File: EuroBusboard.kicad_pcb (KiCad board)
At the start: 2 copper layers, 146 x 70 mm, 39 parts, among them J1 Power In, J10 IDC5, J11 JST5, J12 IDC6, J13 JST6, J14 IDC7, J15 JST7, J16 IDC8, J17 JST8, J18 Power thru, J19 Power In, J2 IDC1, J20 Power thru, J21 Power Thru, J22 Power In, J3 JST1, J4 IDC2, J5 JST2, J6 IDC3, J7 JST3, J8 IDC4, J9 JST4

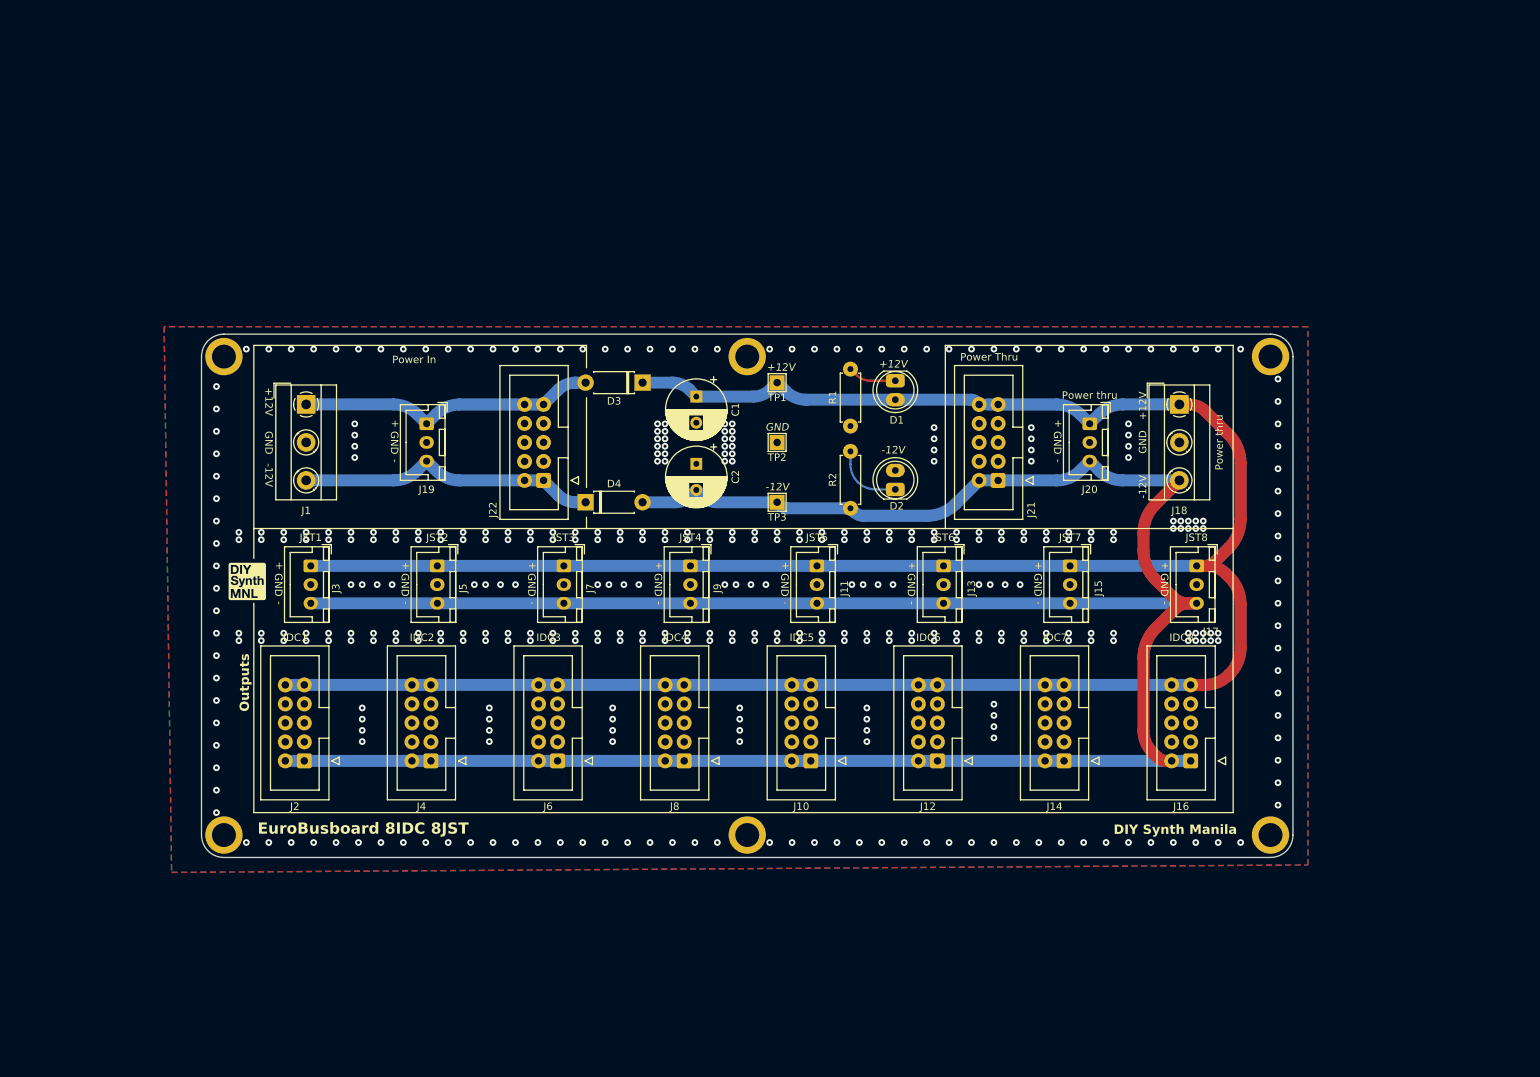
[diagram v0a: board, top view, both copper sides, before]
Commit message: added idc and jst only bus boards
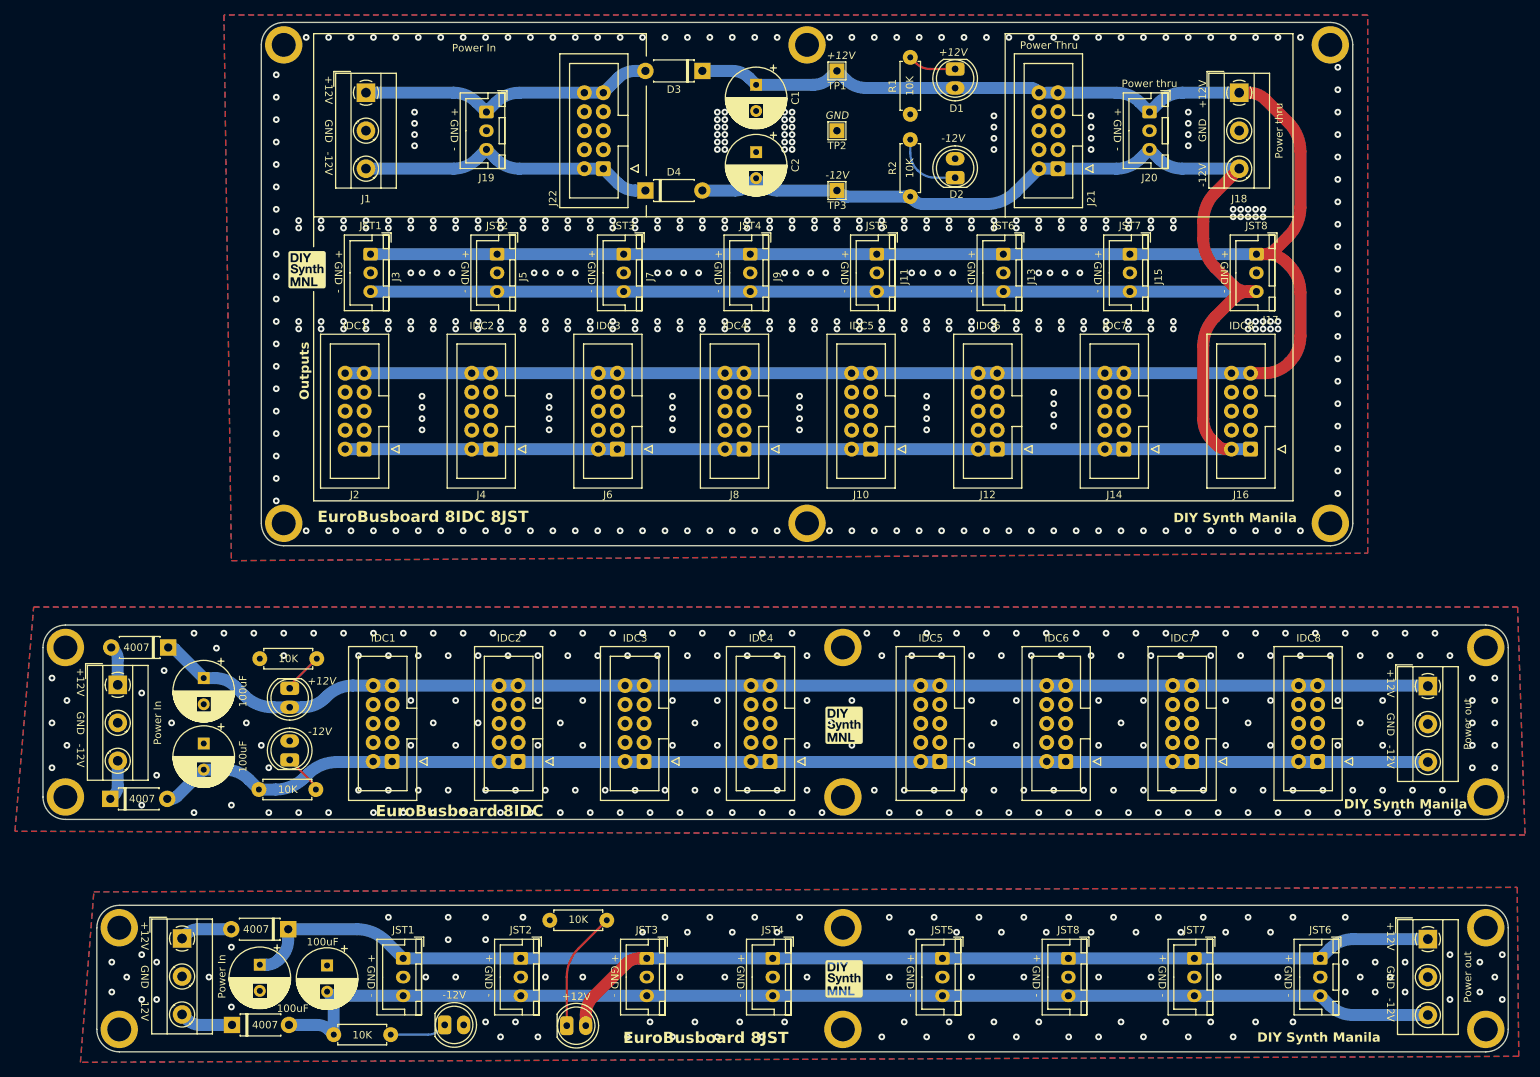
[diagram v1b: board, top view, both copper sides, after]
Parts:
- added B1: Board, PCM_kikit:Board, F.Cu at (86.5, 24.3)
- added B2: Board, PCM_kikit:Board, F.Cu at (58.1, 104.9)
- added B3: Board, PCM_kikit:Board, F.Cu at (64.5, 142.4)
- added C5: 100uF, Capacitor_THT:CP_Radial_D8.0mm_P3.50mm, F.Cu at (82.8, 150.3)
- added C6: 100uF, Capacitor_THT:CP_Radial_D8.0mm_P3.50mm, F.Cu at (91.8, 150.4)
- added C7: 100uF, Capacitor_THT:CP_Radial_D8.0mm_P3.50mm, F.Cu at (75.3, 112.0)
- added C8: 100uF, Capacitor_THT:CP_Radial_D8.0mm_P3.50mm, F.Cu at (75.3, 120.8)
- added D10: 4007, DIYSynthMNL:D_DO-41_SOD81_P7.62mm_Horizontal_BigPads, F.Cu at (79.1, 158.4)
- added D11: +12V, DIYSynthMNL:LED_D5.0mm_BigPads, F.Cu at (125.1, 158.5)
- added D12: -12V, DIYSynthMNL:LED_D5.0mm_BigPads, F.Cu at (108.8, 158.4)
- added D13: +12V, DIYSynthMNL:LED_D5.0mm_BigPads, F.Cu at (86.8, 114.6)
- added D14: 4007, DIYSynthMNL:D_DO-41_SOD81_P7.62mm_Horizontal_BigPads, F.Cu at (70.5, 107.9)
- added D15: -12V, DIYSynthMNL:LED_D5.0mm_BigPads, F.Cu at (86.8, 121.7)
- added D16: 4007, DIYSynthMNL:D_DO-41_SOD81_P7.62mm_Horizontal_BigPads, F.Cu at (62.8, 128.2)
- added D9: 4007, DIYSynthMNL:D_DO-41_SOD81_P7.62mm_Horizontal_BigPads, F.Cu at (86.6, 145.6)
- added H10: MountingHole_Pad, DIYSynthMNL:MountingHole_M3_Standoff_Pad, F.Cu at (160.8, 107.9)
- added H11: MountingHole_Pad, DIYSynthMNL:MountingHole_M3_Standoff_Pad, F.Cu at (56.8, 127.9)
- added H12: MountingHole_Pad, DIYSynthMNL:MountingHole_M3_Standoff_Pad, F.Cu at (246.8, 127.9)
- added H13: MountingHole_Pad, DIYSynthMNL:MountingHole_M3_Standoff_Pad, F.Cu at (246.8, 145.4)
- added H14: MountingHole_Pad, DIYSynthMNL:MountingHole_M3_Standoff_Pad, F.Cu at (246.8, 159.0)
- added H15: MountingHole_Pad, DIYSynthMNL:MountingHole_M3_Standoff_Pad, F.Cu at (160.8, 145.4)
- added H16: MountingHole_Pad, DIYSynthMNL:MountingHole_M3_Standoff_Pad, F.Cu at (160.8, 159.0)
- added H17: MountingHole_Pad, DIYSynthMNL:MountingHole_M3_Standoff_Pad, F.Cu at (64.0, 159.0)
- added H18: MountingHole_Pad, DIYSynthMNL:MountingHole_M3_Standoff_Pad, F.Cu at (64.0, 145.4)
- added H7: MountingHole_Pad, DIYSynthMNL:MountingHole_M3_Standoff_Pad, F.Cu at (56.8, 107.9)
- added H8: MountingHole_Pad, DIYSynthMNL:MountingHole_M3_Standoff_Pad, F.Cu at (160.8, 127.9)
- added H9: MountingHole_Pad, DIYSynthMNL:MountingHole_M3_Standoff_Pad, F.Cu at (246.8, 107.9)
- added J23: IDC1, DIYSynthMNL:IDC-Header_2x05_P2.54mm_Vertical_BigPads, F.Cu at (100.5, 123.2)
- added J24: IDC2, DIYSynthMNL:IDC-Header_2x05_P2.54mm_Vertical_BigPads, F.Cu at (117.4, 123.2)
- added J25: IDC3, DIYSynthMNL:IDC-Header_2x05_P2.54mm_Vertical_BigPads, F.Cu at (134.2, 123.2)
- added J26: IDC4, DIYSynthMNL:IDC-Header_2x05_P2.54mm_Vertical_BigPads, F.Cu at (151.0, 123.2)
- added J27: IDC5, DIYSynthMNL:IDC-Header_2x05_P2.54mm_Vertical_BigPads, F.Cu at (173.8, 123.2)
- added J28: IDC6, DIYSynthMNL:IDC-Header_2x05_P2.54mm_Vertical_BigPads, F.Cu at (190.6, 123.2)
- added J29: IDC7, DIYSynthMNL:IDC-Header_2x05_P2.54mm_Vertical_BigPads, F.Cu at (207.4, 123.2)
- added J30: IDC8, DIYSynthMNL:IDC-Header_2x05_P2.54mm_Vertical_BigPads, F.Cu at (224.3, 123.2)
- added J33: JST1, DIYSynthMNL:Eurorack_power_jst_3P, F.Cu at (102.0, 149.5)
- added J34: JST2, DIYSynthMNL:Eurorack_power_jst_3P, F.Cu at (117.7, 149.5)
- added J35: JST3, DIYSynthMNL:Eurorack_power_jst_3P, F.Cu at (134.6, 149.5)
- added J36: JST4, DIYSynthMNL:Eurorack_power_jst_3P, F.Cu at (151.4, 149.5)
- added J37: JST5, DIYSynthMNL:Eurorack_power_jst_3P, F.Cu at (174.1, 149.5)
- added J38: JST6, DIYSynthMNL:Eurorack_power_jst_3P, F.Cu at (224.7, 149.5)
- added J39: JST7, DIYSynthMNL:Eurorack_power_jst_3P, F.Cu at (207.8, 149.5)
- added J40: JST8, DIYSynthMNL:Eurorack_power_jst_3P, F.Cu at (191.0, 149.5)
- added J41: Power In, DIYSynthMNL:TerminalBlock_MetzConnect_Type101_RT01603HBWC_1x03_P5.08mm_Horizontal, F.Cu at (72.4, 146.8)
- added J42: Power out, DIYSynthMNL:TerminalBlock_MetzConnect_Type101_RT01603HBWC_1x03_P5.08mm_Horizontal, F.Cu at (239.0, 146.9)
- added J43: Power In, DIYSynthMNL:TerminalBlock_MetzConnect_Type101_RT01603HBWC_1x03_P5.08mm_Horizontal, F.Cu at (63.8, 112.9)
- added J44: Power out, DIYSynthMNL:TerminalBlock_MetzConnect_Type101_RT01603HBWC_1x03_P5.08mm_Horizontal, F.Cu at (239.0, 113.1)
- added R5: 10K, DIYSynthMNL:R_quarter_watt_L6.3mm_D2.5mm_P7.62mm, F.Cu at (121.6, 144.4)
- added R6: 10K, DIYSynthMNL:R_quarter_watt_L6.3mm_D2.5mm_P7.62mm, F.Cu at (92.7, 159.7)
- added R7: 10K, DIYSynthMNL:R_quarter_watt_L6.3mm_D2.5mm_P7.62mm, F.Cu at (82.8, 109.4)
- added R8: 10K, DIYSynthMNL:R_quarter_watt_L6.3mm_D2.5mm_P7.62mm, F.Cu at (82.7, 126.9)
- moved C1 42.5 mm to (149.2, 32.6)
- moved C2 42.5 mm to (149.2, 41.6)
- moved D1 42.5 mm to (175.8, 31.8)
- moved D2 42.5 mm to (175.8, 43.8)
- moved D3 42.5 mm to (142.0, 30.8)
- moved D4 42.5 mm to (134.4, 46.8)
- moved H1 42.5 mm to (86.0, 27.3)
- moved H2 42.5 mm to (156.0, 91.3)
- moved H3 42.5 mm to (226.0, 91.3)
- moved H4 42.5 mm to (156.0, 27.3)
- moved H5 42.5 mm to (226.0, 27.3)
- moved H6 42.5 mm to (86.0, 91.3)
- moved J1 42.5 mm to (97.0, 33.7)
- moved J10 42.5 mm to (164.5, 81.4)
- moved J11 42.5 mm to (165.3, 55.3)
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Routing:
- net /EuroBusboard8_JST/+12V_JST: track 0.00 -> 175.1 mm
- net /EuroBusboard8_IDC/+12V_IDC: track 0.00 -> 172.1 mm
- net /EuroBusboard8_IDC/-12V_IDC: track 0.00 -> 172.1 mm
- net /EuroBusboard8_JST/-12V_JST: track 0.00 -> 160.0 mm
- net Net-(D11-K): track 0.00 -> 16.1 mm
- net Net-(D12-K): track 0.00 -> 7.65 mm
- net /EuroBusboard8_JST/-12VIN_JST: track 0.00 -> 7.15 mm
- net /EuroBusboard8_JST/+12VIN_JST: track 0.00 -> 6.99 mm
- net Net-(D13-K): track 0.00 -> 5.44 mm
- net /EuroBusboard8_IDC/-12VIN_IDC: track 0.00 -> 5.42 mm
- net Net-(D15-K): track 0.00 -> 5.38 mm
- net /EuroBusboard8_IDC/+12VIN_IDC: track 0.00 -> 5.29 mm
- net /EuroBusboard8_JST/GND_JST: vias 0 -> 103
- net /EuroBusboard8_IDC/GND_IDC: vias 0 -> 220
- added copper zone on B.Cu, net /EuroBusboard8_IDC/GND_IDC
- added copper zone on F.Cu, net /EuroBusboard8_IDC/GND_IDC
- added copper zone on B.Cu, net /EuroBusboard8_JST/GND_JST
- added copper zone on F.Cu, net /EuroBusboard8_JST/GND_JST
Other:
- board size 146 x 70 mm -> 196 x 137.7 mm
- board text added: "EuroBusboard 8IDC"
- board text added: "EuroBusboard 8JST"
